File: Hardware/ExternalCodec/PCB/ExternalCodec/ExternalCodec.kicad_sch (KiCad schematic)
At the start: 25 parts

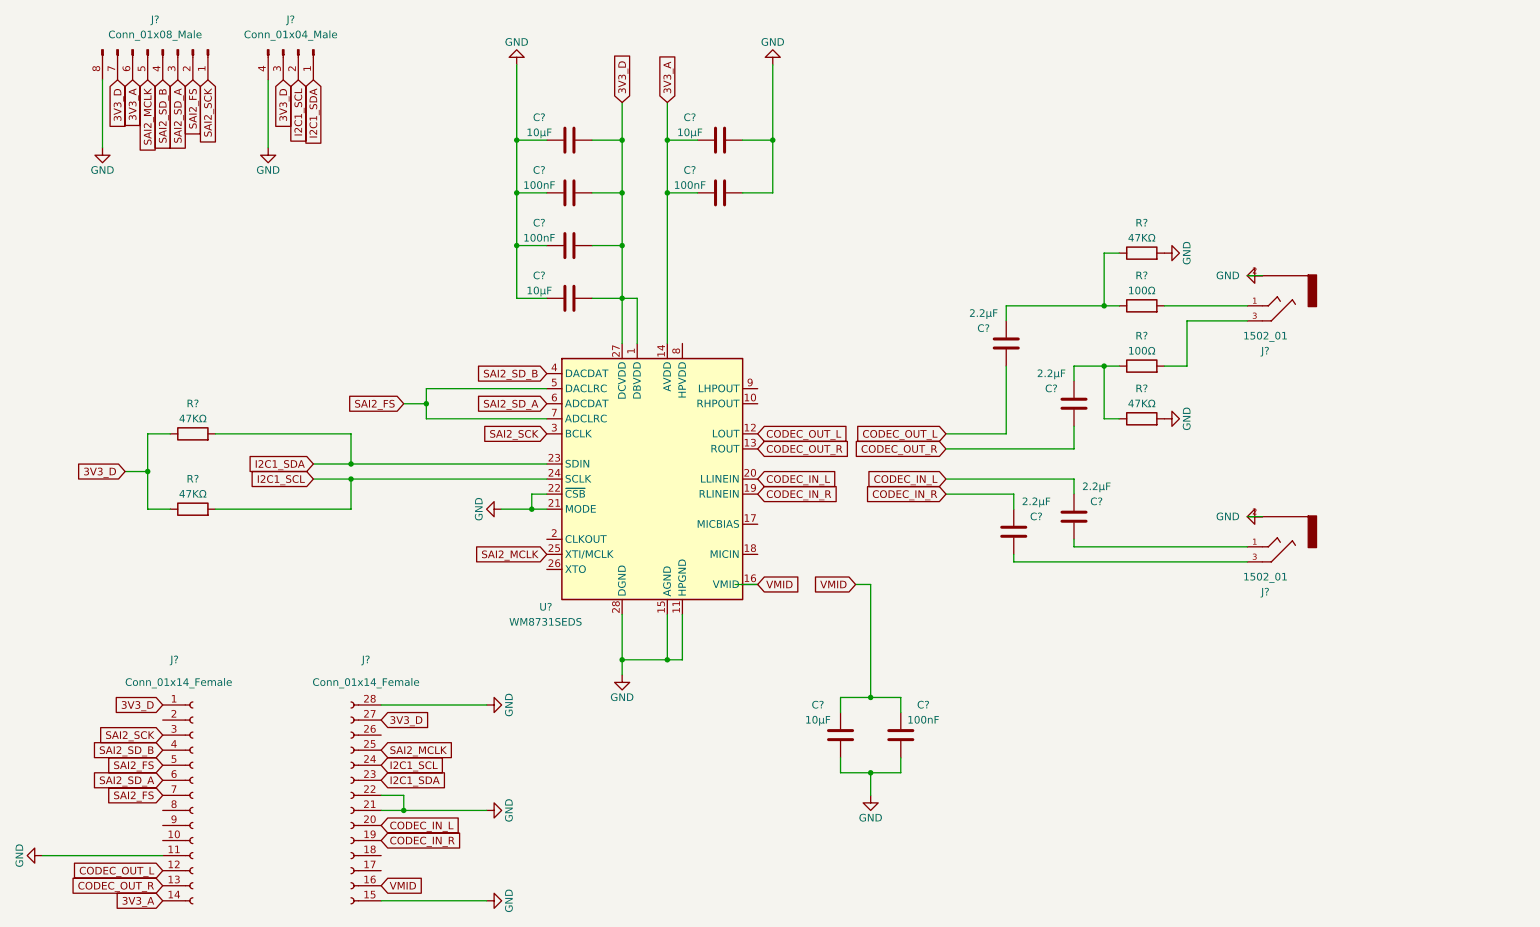
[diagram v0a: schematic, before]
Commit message: Added codec diagram
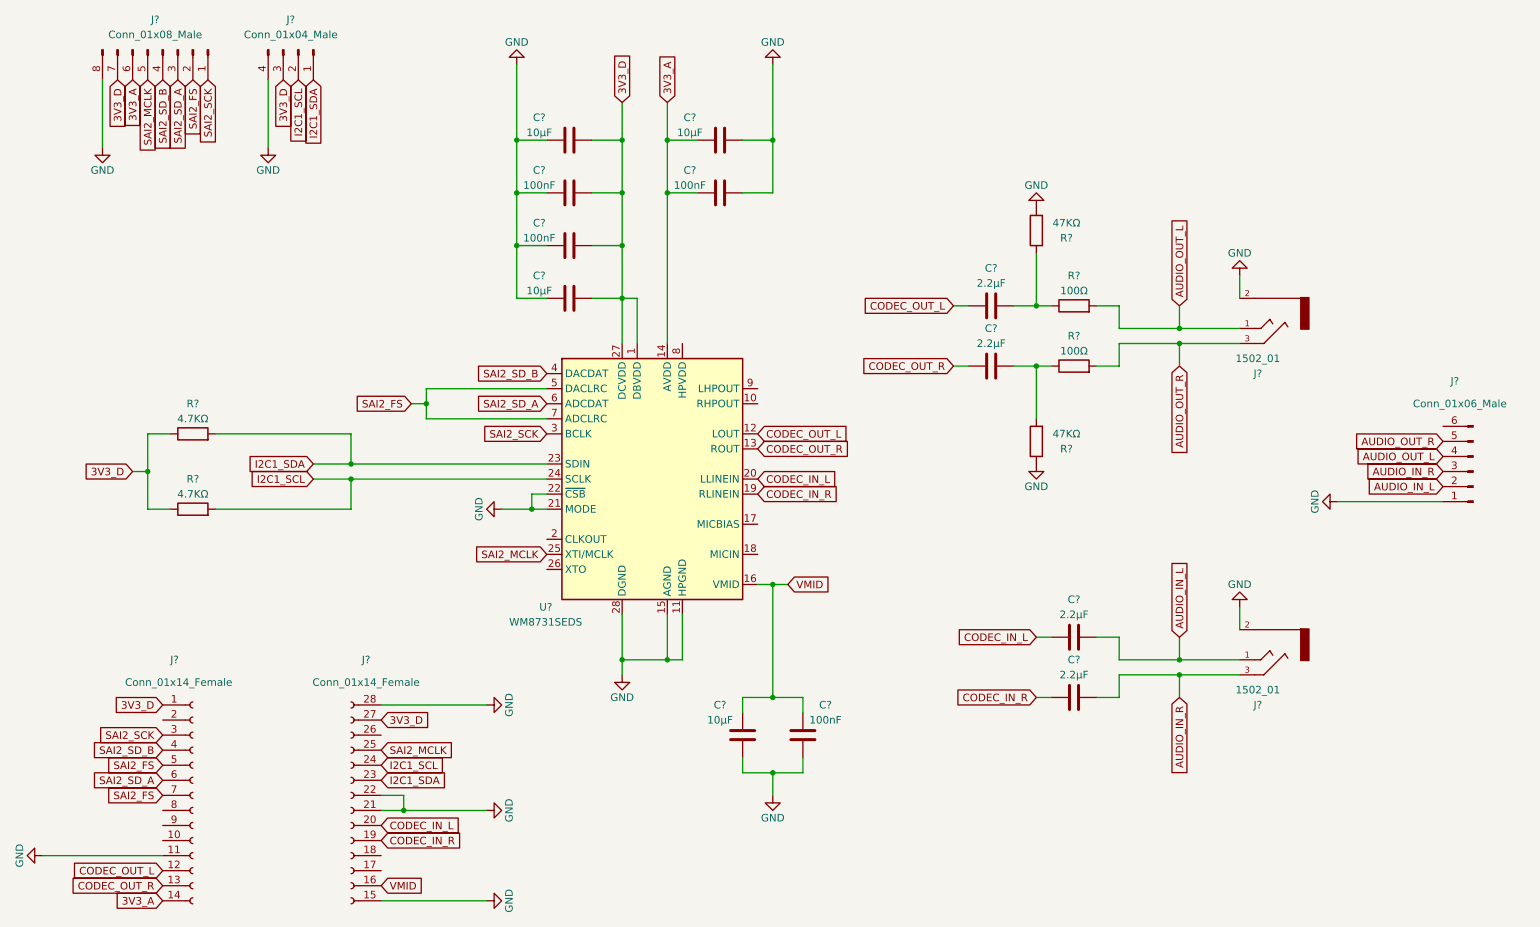
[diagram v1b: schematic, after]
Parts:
- added J?: Conn_01x06_Male, symbol Connector:Conn_01x06_Male
- R? (x2): value 47KΩ -> 4.7KΩ
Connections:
- net CODEC_OUT_L: now also C?.1; no longer C?.2
- net CODEC_OUT_R: now also C?.1; no longer C?.2
- net GND: now also R?.1, J?.1 (Pin_1); no longer R?.2
- net at R?.1, R?.1: now also C?.2; no longer C?.1
- net AUDIO_OUT_R: now reaches J?.3, R?.2
- net AUDIO_OUT_R: now also J?.5 (Pin_5)
- net AUDIO_IN_L: now reaches C?.2, J?.1
- net AUDIO_IN_L: now also J?.2 (Pin_2)
- net AUDIO_IN_R: now reaches C?.2, J?.3
- net AUDIO_IN_R: now also J?.3 (Pin_3)
- net AUDIO_OUT_L: now reaches J?.1, R?.2
- net AUDIO_OUT_L: now also J?.4 (Pin_4)
- new net: C?.2, R?.1, R?.2
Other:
- title: Daisy Seed Development Kit ExternalCodec -> Daisy Seed Development Kit External Codec
- moved on the sheet: C?, J?, R?

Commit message: External codec Kicad files added
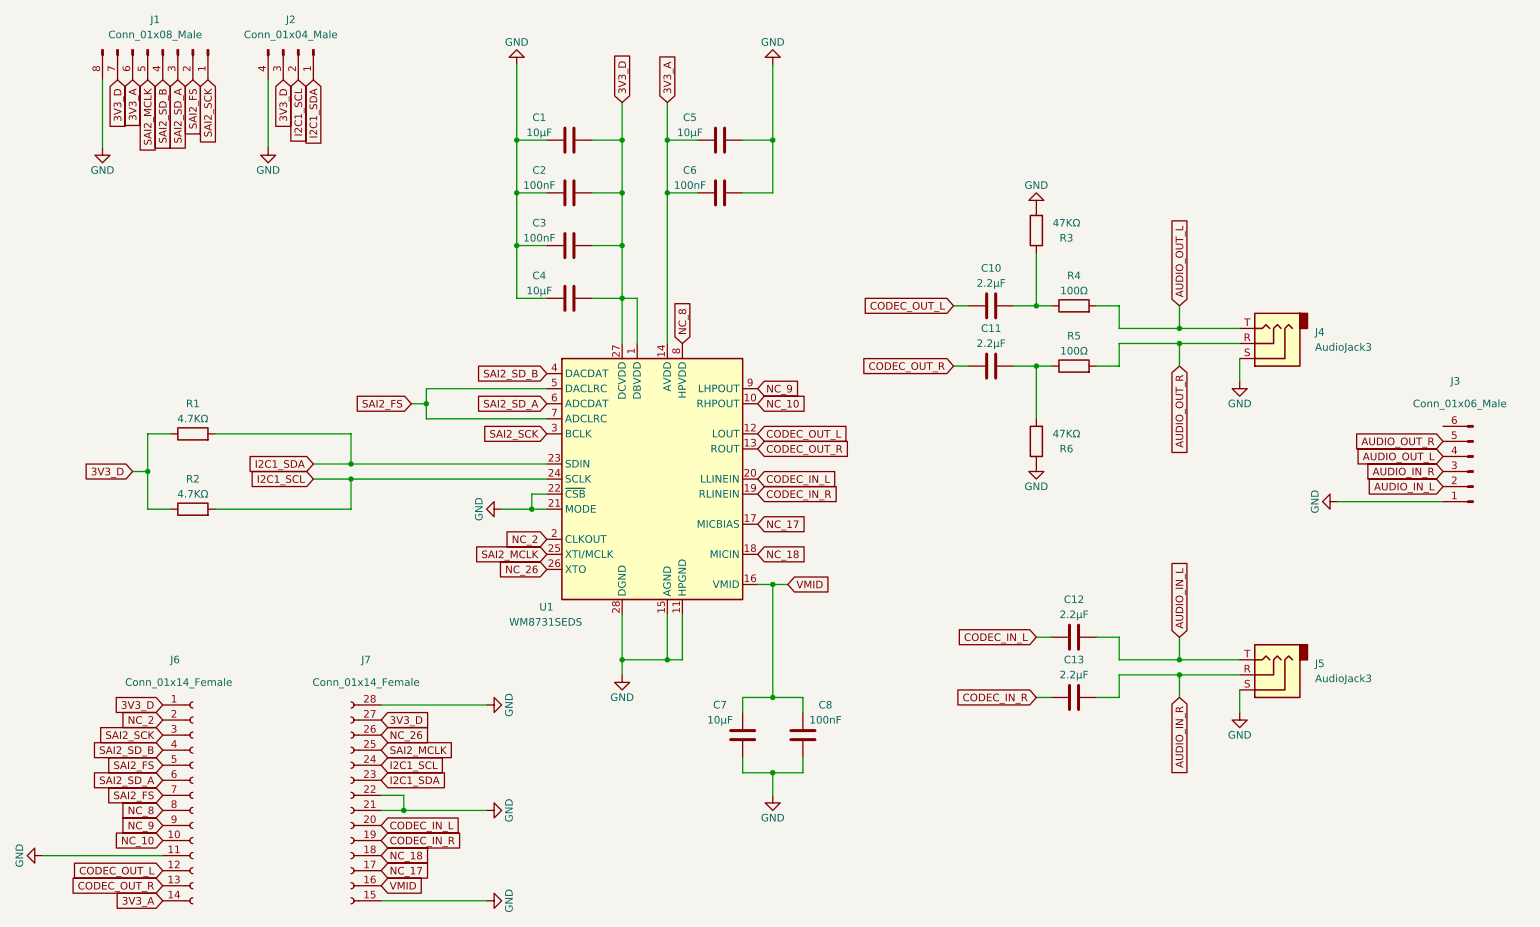
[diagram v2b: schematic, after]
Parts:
- removed J? (x2): 1502_01, 1502_01:1502_01, symbol 1502_01:1502_01
- added J4, J5: AudioJack3, Protoplasma.pretty:PJ-307, symbol Connector:AudioJack3
- C1, C10, C11, C12, C13, C4, C5, C7: renamed from C?; footprint (none) -> Capacitor_THT:C_Disc_D5.0mm_W2.5mm_P5.00mm
- C2, C3, C6, C8: renamed from C?; footprint (none) -> Capacitor_THT:C_Disc_D5.0mm_W2.5mm_P2.50mm
- J2: renamed from J?; footprint (none) -> Connector_PinSocket_2.54mm:PinSocket_1x04_P2.54mm_Vertical
- J3: renamed from J?; footprint (none) -> Connector_PinSocket_2.54mm:PinSocket_1x06_P2.54mm_Vertical
- J6, J7: renamed from J?; footprint (none) -> Connector_PinSocket_2.54mm:PinSocket_1x14_P2.54mm_Vertical
- R1, R2, R3, R4, R5, R6: renamed from R?; footprint (none) -> Resistor_THT:R_Axial_DIN0207_L6.3mm_D2.5mm_P10.16mm_Horizontal
- gave numbers to parts that had none: 2
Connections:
- net AUDIO_IN_L: now also J5.T
- net AUDIO_IN_R: now also J5.R
- net AUDIO_OUT_L: now also J4.T
- net AUDIO_OUT_R: now also J4.R
- net GND: now also J4.S, J5.S
- net NC_10: now reaches U1.10 (RHPOUT)
- net NC_10: now also J6.10 (Pin_10)
- net NC_17: now reaches U1.17 (MICBIAS)
- net NC_17: now also J7.17 (Pin_3)
- net NC_18: now reaches U1.18 (MICIN)
- net NC_18: now also J7.18 (Pin_4)
- net NC_2: now reaches U1.2 (CLKOUT)
- net NC_2: now also J6.2 (Pin_2)
- net NC_26: now reaches U1.26 (XTO)
- net NC_26: now also J7.26 (Pin_12)
- net NC_8: now reaches U1.8 (HPVDD)
- net NC_8: now also J6.8 (Pin_8)
- net NC_9: now reaches U1.9 (LHPOUT)
- net NC_9: now also J6.9 (Pin_9)
